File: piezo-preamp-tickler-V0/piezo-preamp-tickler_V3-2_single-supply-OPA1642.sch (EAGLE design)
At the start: 30 parts, among them IC1 OPA1612, Q2 MMBFJ201, SW1-INPUT SPDTCSS-1210B, SW1-OUTPUT SWITCH_DPDT

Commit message: new piezo preamp designs
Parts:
- removed D2: 1N4148W, CMU-ArtFab:ZENER-DIOD
- added C15, C16, C18, C20: 10uF, adafruit:C-USC0805K
- added C17, C21, C8: 0.1uF, adafruit:C-USC0805K
- added C19: 22pF, adafruit:C-USC0805K
- added D4: 1N4148, adafruit:DIODESOD-123
- added D5: 10BQ015, SparkFun:DIODESMA
- added J4: Battery, SparkFun-Connectors:CONN_02LOCK
- added J5: (no value), SparkFun-Connectors:USB_MICRO-BREDUCED_PASTE
- added J6, J7: 12V, SparkFun-Connectors:CONN_02
- added L3: 2.7 uH, SparkFun-Coils:INDUCTOR-CR54-3.3UH
- added LED4, LED5: (no value), led:LED3MM
- added Q1: BQ21040, CMU-ArtFab:BQ21040-LIPO-CHARGER
- added Q7: BQ297X, CMU-ArtFab:BQ297X-BATTERY-MANAGER
- added Q8: DMN2400, CMU-ArtFab:DUAL-NFET-DMN2400
- added Q9: SC4503, CMU-ArtFab:SC4503
- added R16: 866k, CMU-ArtFab:R-US_R0805
- added R17: 100k, CMU-ArtFab:R-US_R0805
- added R26: 15k, CMU-ArtFab:R-US_R0805
- added R27: 1k, CMU-ArtFab:R-US_R0805
- added R28, R29: 10k, CMU-ArtFab:R-US_R0805
- added R30: 330, CMU-ArtFab:R-US_R0805
- added R4: 390, CMU-ArtFab:R-US_R0805
- added R5: 10, CMU-ArtFab:R-US_R0805
- added SW1: SPDT, CMU-ArtFab:SWITCH_SPDTCL-SB-12B
- D1: value 1N4148W -> BAT54S; device CMU-ArtFab:ZENER-DIOD -> diode:BAT54S
- IC1: value OPA1612 -> OPA1642
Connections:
- removed net N$4: D1.A, D2.A
- new net GND2: C16.2, C17.2, J5.GND, Q1.GND, Q7.VSS, Q8.D1, R28.1, R29.1, SW1.2
- new net N$13: LED4.A, R4.1
- new net N$14: J4.2, SW1.1
- new net N$15: D5.A, L3.2, Q9.SW
- new net N$17: C21.1, Q9.SHDN, R26.1
- new net N$19: C19.2, Q9.FB, R16.1, R17.2
- new net N$20: LED5.C, R27.1
- new net N$25: Q1.CHG, R27.2
- new net N$26: Q1.TS, R28.2
- new net N$27: Q1.CURRENT-SET, R29.2
- new net N$28: C17.1, Q7.BAT, R30.2
- new net N$36: Q8.D2, Q8.S1
- new net N$42: Q7.CHG-FET, Q8.G1
- new net N$47: Q7.DRAIN-FET, Q8.G2
- new net N$48: C15.1, D4.C, R5.2
- new net N$49: C8.1, J6.2, J7.2, R5.1
- new net V+: C16.1, J5.VBUS, LED5.A, Q1.VIN
- new net VBAT: C18.1, J4.1, L3.1, Q1.OUT, Q9.IN, R26.2, R30.1, R4.2
- net +12V: now also C19.1, C20.1, D4.A, D5.C, R16.2
- net GND: now also C15.2, C18.2, C20.2, C21.2, C8.2, D1.A1, J6.1, J7.1, LED4.C, Q7.V-, Q8.S2, Q9.GND, R17.1; no longer D2.C
- net N$32: now also D1.C2
- net N$5: now also D1.C1A2; no longer D1.C
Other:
- note added: "Battery Charging"
- note added: "DIODE ZENER 5.1V 500MW SOD123"
- note added: "First Stage: Over-voltage protection"
- note added: "Power"
- note added: "Second Stage: OpAmp Amplification"
- note added: "Third Stage: FET-buffer, for mobile phone input"
- note added: "Voltage Regulation"

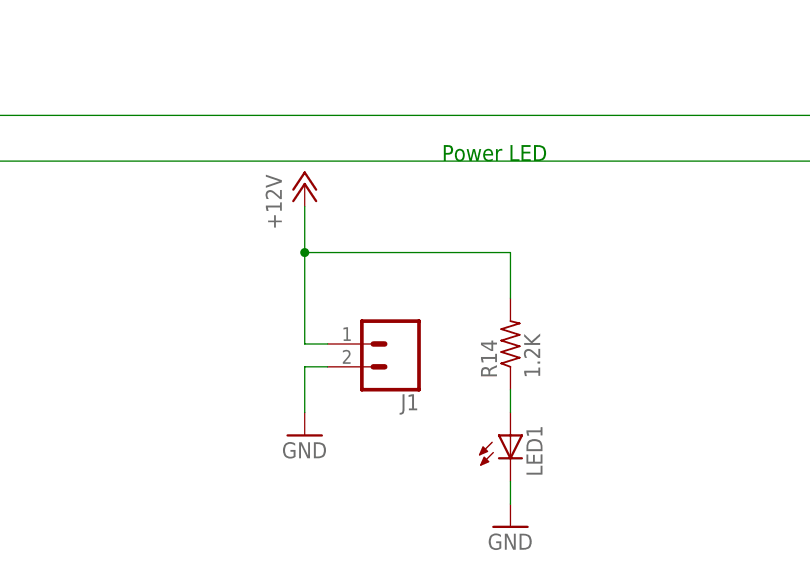
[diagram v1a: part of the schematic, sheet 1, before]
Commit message: new piezo preamp circuit v3-3 added
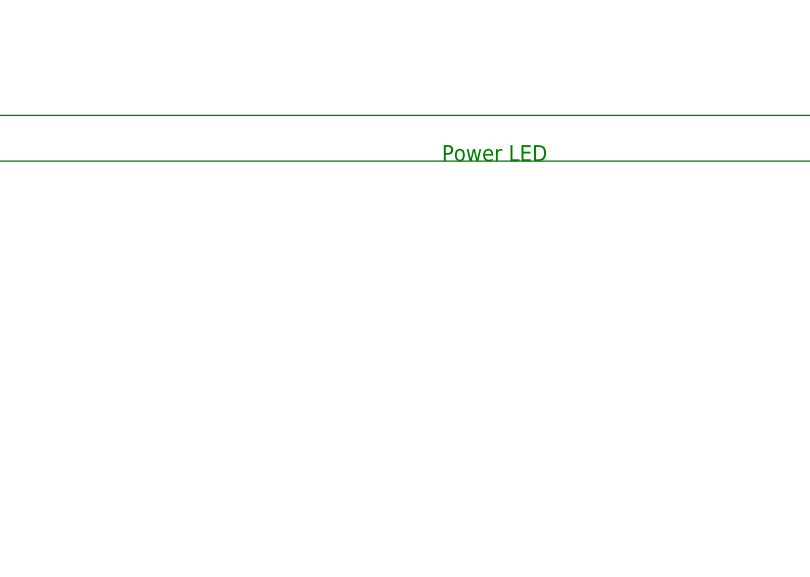
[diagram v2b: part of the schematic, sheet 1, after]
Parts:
- removed J1: (no value), SparkFun-Connectors:CONN_02LOCK
- removed LED1: (no value), led:LED3MM
- removed R14: 1.2K, CMU-ArtFab:R-US_R0603
- added J2: (no value), SparkFun-Connectors:CONN_02LOCK
- added LED2: (no value), led:LED3MM
- added R3: 1.2K, CMU-ArtFab:R-US_R0603
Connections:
- removed net N$2: LED1.A, R14.1
- new net N$4: LED2.A, R3.1
- net +12V: now also J2.1, R3.2; no longer J1.1, R14.2
- net GND: now also J2.2, LED2.C; no longer J1.2, LED1.C
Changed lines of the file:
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@@
 <part name="SUPPLY2" library="supply2" library_urn="urn:adsk.eagle:library:372" deviceset="GND" device=""/>
 <part name="C2" library="rcl" library_urn="urn:adsk.eagle:library:334" deviceset="C-US" device="C1206" package3d_urn="urn:adsk.eagle:package:23618/2" value="10uF"/>
-<part name="J1" library="SparkFun-Connectors" library_urn="urn:adsk.eagle:library:513" deviceset="CONN_02" device="LOCK"/>
-<part name="P+2" library="supply1" library_urn="urn:adsk.eagle:library:371" deviceset="+12V" device=""/>
-<part name="GND7" library="supply1" library_urn="urn:adsk.eagle:library:371" deviceset="GND" device=""/>
 <part name="HEADSET" library="CMU-ArtFab" deviceset="TRRS-3.5MM" device="LGPADS" value="SJ-43514"/>
 <part name="PHONE" library="CMU-ArtFab" deviceset="TRRS-3.5MM" device="LGPADS" value="SJ-43514"/>
-<part name="LED1" library="led" library_urn="urn:adsk.eagle:library:259" deviceset="LED" device="3MM"/>
-<part name="GND8" library="supply1" library_urn="urn:adsk.eagle:library:371" deviceset="GND" device=""/>
-<part name="R14" library="CMU-ArtFab" deviceset="R-US_" device="R0603" value="1.2K"/>
 <part name="R15" library="CMU-ArtFab" deviceset="POT" device="TRIMPOT-MULTI" value="20K"/>
 <part name="C3" library="microbuilder" deviceset="CAP_TANTALUM" device="D/7343_REFLOW" value="100uF"/>
@@
 <part name="L3" library="SparkFun-Coils" deviceset="INDUCTOR" device="-CR54-3.3UH" value="2.7 uH"/>
 <part name="D1" library="diode" library_urn="urn:adsk.eagle:library:210" deviceset="BAT54S" device="" package3d_urn="urn:adsk.eagle:package:43389/2"/>
+<part name="J2" library="SparkFun-Connectors" library_urn="urn:adsk.eagle:library:513" deviceset="CONN_02" device="LOCK"/>
+<part name="P+3" library="supply1" library_urn="urn:adsk.eagle:library:371" deviceset="+12V" device=""/>
+<part name="GND6" library="supply1" library_urn="urn:adsk.eagle:library:371" deviceset="GND" device=""/>
+<part name="LED2" library="led" library_urn="urn:adsk.eagle:library:259" deviceset="LED" device="3MM"/>
+<part name="GND9" library="supply1" library_urn="urn:adsk.eagle:library:371" deviceset="GND" device=""/>
+<part name="R3" library="CMU-ArtFab" deviceset="R-US_" device="R0603" value="1.2K"/>
 </parts>
 <sheets>
@@
 <instance part="SUPPLY2" gate="GND" x="220.98" y="-109.22"/>
 <instance part="C2" gate="G$1" x="-27.94" y="-78.74"/>
-<instance part="J1" gate="G$1" x="144.78" y="-149.86" rot="R180"/>
-<instance part="P+2" gate="1" x="134.62" y="-132.08"/>
-<instance part="GND7" gate="1" x="134.62" y="-160.02" smashed="yes">
-<attribute name="VALUE" x="132.08" y="-162.56" size="1.778" layer="96" ratio="12"/>
-</instance>
 <instance part="HEADSET" gate="G$1" x="264.16" y="-35.56" rot="R180"/>
 <instance part="PHONE" gate="G$1" x="264.16" y="-55.88" rot="R180"/>
-<instance part="LED1" gate="G$1" x="157.48" y="-160.02"/>
-<instance part="GND8" gate="1" x="157.48" y="-170.18" smashed="yes">
-<attribute name="VALUE" x="154.94" y="-172.72" size="1.778" layer="96" ratio="12"/>
-</instance>
-<instance part="R14" gate="G$1" x="157.48" y="-149.86" rot="R90"/>
 <instance part="R15" gate="G$1" x="7.62" y="-104.14"/>
 <instance part="C3" gate="G$1" x="-20.32" y="-96.52" rot="R90"/>
@@
 <junction x="220.98" y="-96.52"/>
 </segment>
-<segment>
-<pinref part="J1" gate="G$1" pin="2"/>
-<pinref part="GND7" gate="1" pin="GND"/>
-<wire x1="137.16" y1="-152.4" x2="134.62" y2="-152.4" width="0.1524" layer="91"/>
-<wire x1="134.62" y1="-152.4" x2="134.62" y2="-157.48" width="0.1524" layer="91"/>
-</segment>
-<segment>
-<pinref part="LED1" gate="G$1" pin="C"/>
-<pinref part="GND8" gate="1" pin="GND"/>
-<wire x1="157.48" y1="-165.1" x2="157.48" y2="-167.64" width="0.1524" layer="91"/>
-</segment>
 </net>
 <net name="+12V" class="0">
@@
 <wire x1="30.48" y1="-43.18" x2="30.48" y2="-45.72" width="0.1524" layer="91"/>
 <pinref part="L1" gate="G$1" pin="1"/>
-</segment>
-<segment>
-<pinref part="J1" gate="G$1" pin="1"/>
-<pinref part="P+2" gate="1" pin="+12V"/>
-<wire x1="137.16" y1="-149.86" x2="134.62" y2="-149.86" width="0.1524" layer="91"/>
-<wire x1="134.62" y1="-149.86" x2="134.62" y2="-139.7" width="0.1524" layer="91"/>
-<pinref part="R14" gate="G$1" pin="2"/>
-<wire x1="134.62" y1="-139.7" x2="134.62" y2="-134.62" width="0.1524" layer="91"/>
-<wire x1="134.62" y1="-139.7" x2="157.48" y2="-139.7" width="0.1524" layer="91"/>
-<wire x1="157.48" y1="-139.7" x2="157.48" y2="-144.78" width="0.1524" layer="91"/>
-<junction x="134.62" y="-139.7"/>
 </segment>
 </net>
@@
 <wire x1="83.82" y1="-73.66" x2="106.68" y2="-73.66" width="0.1524" layer="91"/>
 <wire x1="106.68" y1="-73.66" x2="106.68" y2="-76.2" width="0.1524" layer="91"/>
-</segment>
-</net>
-<net name="N$2" class="0">
-<segment>
-<pinref part="R14" gate="G$1" pin="1"/>
-<pinref part="LED1" gate="G$1" pin="A"/>
-<wire x1="157.48" y1="-154.94" x2="157.48" y2="-157.48" width="0.1524" layer="91"/>
 </segment>
 </net>
@@
 <instance part="SUPPLY9" gate="GND" x="86.36" y="193.04" rot="R180"/>
 <instance part="SUPPLY10" gate="GND" x="73.66" y="193.04" rot="R180"/>
+<instance part="J2" gate="G$1" x="152.4" y="193.04" rot="R180"/>
+<instance part="P+3" gate="1" x="142.24" y="210.82"/>
+<instance part="GND6" gate="1" x="142.24" y="182.88" smashed="yes">
+<attribute name="VALUE" x="139.7" y="180.34" size="1.778" layer="96" ratio="12"/>
+</instance>
+<instance part="LED2" gate="G$1" x="165.1" y="182.88"/>
+<instance part="GND9" gate="1" x="165.1" y="172.72" smashed="yes">
+<attribute name="VALUE" x="162.56" y="170.18" size="1.778" layer="96" ratio="12"/>
+</instance>
+<instance part="R3" gate="G$1" x="165.1" y="193.04" rot="R90"/>
 </instances>
 <busses>
@@
 <pinref part="J6" gate="G$1" pin="1"/>
 <wire x1="73.66" y1="190.5" x2="73.66" y2="187.96" width="0.1524" layer="91"/>
+</segment>
+<segment>
+<pinref part="J2" gate="G$1" pin="2"/>
+<pinref part="GND6" gate="1" pin="GND"/>
+<wire x1="144.78" y1="190.5" x2="142.24" y2="190.5" width="0.1524" layer="91"/>
+<wire x1="142.24" y1="190.5" x2="142.24" y2="185.42" width="0.1524" layer="91"/>
+</segment>
+<segment>
+<pinref part="LED2" gate="G$1" pin="C"/>
+<pinref part="GND9" gate="1" pin="GND"/>
+<wire x1="165.1" y1="177.8" x2="165.1" y2="175.26" width="0.1524" layer="91"/>
 </segment>
 </net>
@@
 <wire x1="25.4" y1="203.2" x2="25.4" y2="195.58" width="0.1524" layer="91"/>
 <wire x1="25.4" y1="195.58" x2="30.48" y2="195.58" width="0.1524" layer="91"/>
+</segment>
+<segment>
+<pinref part="J2" gate="G$1" pin="1"/>
+<pinref part="P+3" gate="1" pin="+12V"/>
+<wire x1="144.78" y1="193.04" x2="142.24" y2="193.04" width="0.1524" layer="91"/>
+<wire x1="142.24" y1="193.04" x2="142.24" y2="203.2" width="0.1524" layer="91"/>
+<pinref part="R3" gate="G$1" pin="2"/>
+<wire x1="142.24" y1="203.2" x2="142.24" y2="208.28" width="0.1524" layer="91"/>
+<wire x1="142.24" y1="203.2" x2="165.1" y2="203.2" width="0.1524" layer="91"/>
+<wire x1="165.1" y1="203.2" x2="165.1" y2="198.12" width="0.1524" layer="91"/>
+<junction x="142.24" y="203.2"/>
 </segment>
 </net>
@@
 </segment>
 </net>
+<net name="N$4" class="0">
+<segment>
+<pinref part="R3" gate="G$1" pin="1"/>
+<pinref part="LED2" gate="G$1" pin="A"/>
+<wire x1="165.1" y1="187.96" x2="165.1" y2="185.42" width="0.1524" layer="91"/>
+</segment>
+</net>
